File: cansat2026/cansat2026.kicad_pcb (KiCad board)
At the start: 4 copper layers, 82 x 70 mm, 252 parts, among them J101 MCU_UART_Conn, J102 CAM_Conn, J103 I2C_Conn, J104 MCU_Power, J105 MCU_Power, J106 Micro_SD_Card_Det_Hirose_DM3AT, J1101 USB_C_Receptacle_USB2.0_14P, J201 FlightPin, J301 Battery, J302 Battery, J401 M1, J402 M2, J403 M3, J801 Conn_Coaxial, Q1101 2N7002, Q1102 2N7002, Q301 2SB1198K, Q302 2SB1198K, Q303 2N7002, Q304 2SB1198K, Q305 2N7002, Q306 2SC2412K, Q307 PJA3404A, Q308 PJA3404A, SW201 SW_SPST, SW901 SW_SPST, U1001 ICE40UP5K-SG48ITR, U101 E220-900T22S(JP), U1101 USBLC6-2SC6, U1102 CH340K, U201 TPS70912DRVR, U202 TCR2LN18, U203 TPS561201DDC, U204 74HC08, U205 INA226, U206 TPS562242, U207 XC6206P332MR, U208 TPS62180, U209 TPS62180, U210 TPS63070, U301 S-8209ABB-T8T1U, U302 S-8209ABB-T8T1U, U401 TC78H653FTG, U402 TC78H653FTG, U403 AM8068, U601 HP203B, U701 LSM6DSV, U801 MAX-M10S, U901 ESP32-S3-WROOM-1U-N4R8, U902 AW9523B

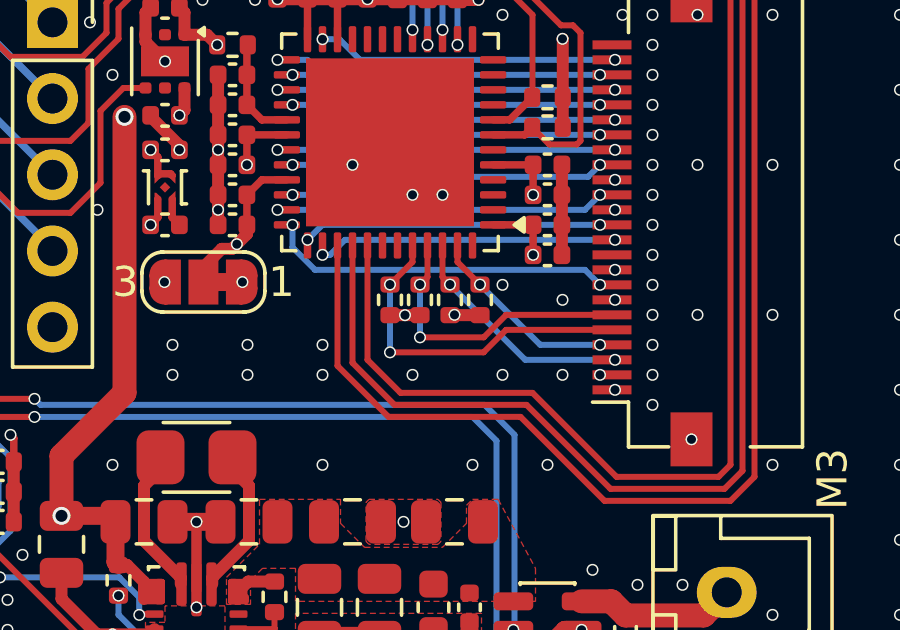
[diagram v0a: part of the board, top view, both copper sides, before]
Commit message: カメラのSCCBのPUをDNPに
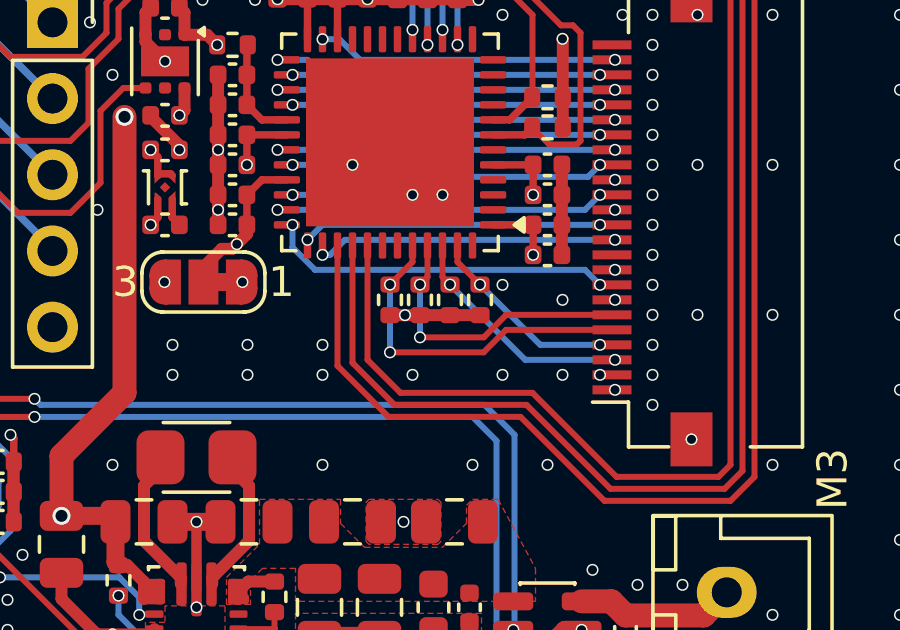
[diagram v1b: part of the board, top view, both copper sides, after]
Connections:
- R912 pad 1: /VCC -> /1.8V
- R913 pad 1: /VCC -> /1.8V
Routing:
- net /1.8V: track 11.7 -> 13.7 mm
- net /VCC: track 100.0 -> 99.1 mm, vias 35 -> 34
